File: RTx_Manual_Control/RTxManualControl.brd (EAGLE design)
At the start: 160 x 100 mm, 15 parts

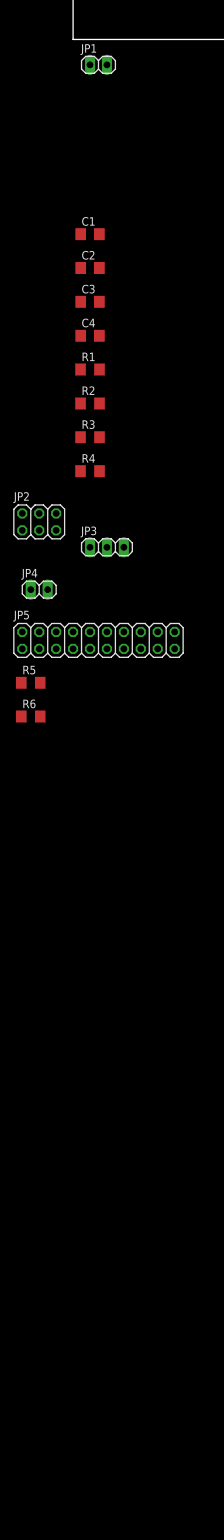
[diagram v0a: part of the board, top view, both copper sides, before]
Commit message: Completed draft of schematic without LPF component values. Need to determine LPF values, verify processor pinouts.
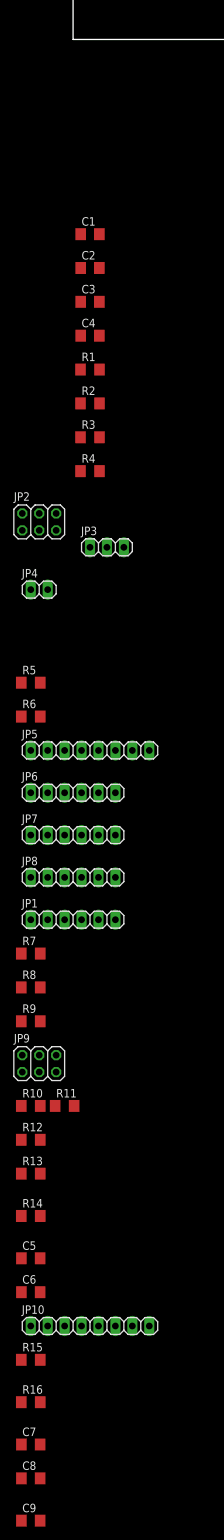
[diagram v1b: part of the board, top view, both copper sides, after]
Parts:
- added C5, C6: (no value), rcl:C1206
- added C7, C8, C9: 1uF, rcl:C1206
- added JP10: CON3, pinhead:1X08
- added JP6: CON2, pinhead:1X06
- added JP7: Main Axis Inputs, pinhead:1X06
- added JP8: Aux Axis Inputs, pinhead:1X06
- added JP9: Aux Switch/LEDs, pinhead:2X03
- added R10, R11, R7, R8: (no value), rcl:R1206
- added R12, R13, R9: 1k, rcl:R1206
- added R14, R15, R16: 10k, rcl:R1206
- JP1: value (none) -> CON1; device pinhead:1X02 -> pinhead:1X06
- JP2: value (none) -> Mode Switch/LEDs
- JP3: value (none) -> Neutral LEDs
- JP4: value (none) -> Drive Enable
- JP5: value (none) -> CON4; device pinhead:2X10 -> pinhead:1X08
- moved JP1 128.3 mm to (0.00, -132.1)
- moved JP5 16.6 mm to (2.54, -106.7)
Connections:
- removed net CH1_ADC: C1.1, R1.2
- removed net CH2_ADC: C2.1, R2.2
- removed net CH3_ADC: C3.1, R3.2
- removed net CH4_ADC: C4.1, R4.2
- removed net N$1: JP3.3, R6.2
- removed net N$2: JP3.2, R5.2
- new net +3.3V: C5.1, JP1.2, R12.2, R13.2, R9.2
- new net AREF: JP5.1, JP7.3, JP7.4, JP8.3, JP8.4
- new net AUX1_LED: JP6.1, R10.2
- new net AUX1_LED_CONN: JP9.2, R10.1
- new net AUX2_LED: JP6.4, R11.2
- new net AUX2_LED_CONN: JP9.6, R11.1
- new net AUX_SWITCH_IN: C7.1, JP10.6, JP9.1, R15.2
- new net AUX_SWITCH_PULLUP: JP9.3, R12.1
- new net AXIS3_ADC: C3.1, JP6.2, R3.2
- new net AXIS3_CONN: JP8.5, R3.1
- new net AXIS4_ADC: C4.1, JP6.3, R4.2
- new net AXIS4_CONN: JP8.2, R4.1
- new net DRIVE_ENABLE_IN: C9.1, JP4.2, JP5.4, R14.2
- new net DRIVE_ENABLE_PULLUP: JP4.1, R13.1
- new net LAT_AXIS_ADC: C2.1, JP5.6, R2.2
- new net LAT_AXIS_CONN: JP7.2, R2.1
- new net LAT_NEAUTRAL_LED_CONN: JP3.3, R6.1
- new net LAT_NEUTRAL_LED: JP6.6, R6.2
- new net MODE1_LED: JP5.7, R7.2
- new net MODE1_LED_CONN: JP2.2, R7.1
- new net MODE2_LED: JP5.8, R8.2
- new net MODE2_LED_CONN: JP2.6, R8.1
- new net MODE_SWITCH_IN: C8.1, JP10.4, JP2.5, R16.2
- new net MODE_SWITCH_PULLUP: JP2.3, R9.1
- new net VERT_AXIS_ADC: C1.1, JP5.3, R1.2
- new net VERT_AXIS_CONN: JP7.5, R1.1
- new net VERT_NEUTRAL_LED: JP6.5, R5.2
- new net VERT_NEUTRAL_LED_CONN: JP3.2, R5.1
- net +5V: now also C6.1, JP1.3, JP2.4, JP9.4
- net GND: now also C5.2, C6.2, C7.2, C8.2, C9.2, JP1.4, JP1.5, JP5.2, JP7.1, JP7.6, JP8.1, JP8.6, R14.1, R15.1, R16.1

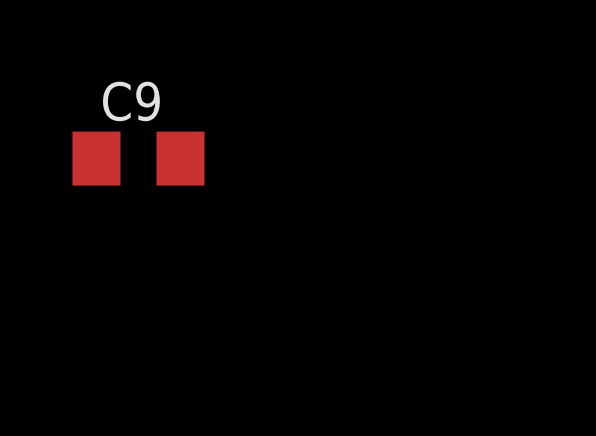
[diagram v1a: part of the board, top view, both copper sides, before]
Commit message: Changed pinout of Neutral LED connector. Added supply rail decoupling cap values, ARef decoupling cap.
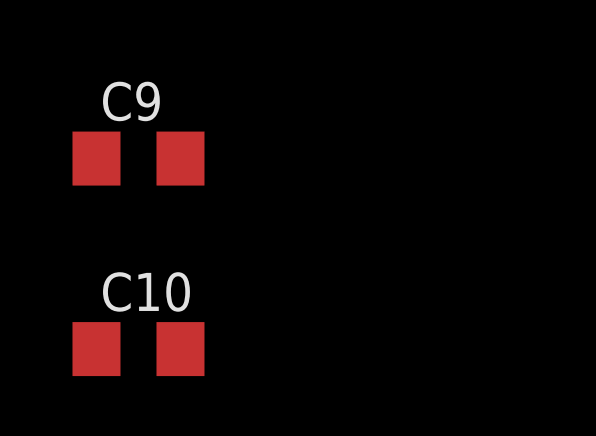
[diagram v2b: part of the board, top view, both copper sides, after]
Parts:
- added C10: 10uF, rcl:C1206
- C5, C6: value (none) -> 10uF
- R10, R11, R5, R6, R7, R8: value (none) -> 280
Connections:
- net +5V: now also JP3.2; no longer JP3.1
- net AREF: now also C10.1
- net GND: now also C10.2
- net VERT_NEUTRAL_LED_CONN: now also JP3.1; no longer JP3.2
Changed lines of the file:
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@@
 <element name="JP2" library="pinhead" package="2X03" value="Mode Switch/LEDs" x="-5.08" y="-72.39"/>
 <element name="JP4" library="pinhead" package="1X02" value="Drive Enable" x="-5.08" y="-82.55"/>
-<element name="R5" library="rcl" package="R1206" value="" x="-6.35" y="-96.52"/>
-<element name="R6" library="rcl" package="R1206" value="" x="-6.35" y="-101.6"/>
+<element name="R5" library="rcl" package="R1206" value="280" x="-6.35" y="-96.52"/>
+<element name="R6" library="rcl" package="R1206" value="280" x="-6.35" y="-101.6"/>
 <element name="JP5" library="pinhead" package="1X08" value="CON4" x="2.54" y="-106.68"/>
 <element name="JP6" library="pinhead" package="1X06" value="CON2" x="0" y="-113.03"/>
@@
 <element name="JP8" library="pinhead" package="1X06" value="Aux Axis Inputs" x="0" y="-125.73"/>
 <element name="JP1" library="pinhead" package="1X06" value="CON1" x="0" y="-132.08"/>
-<element name="R7" library="rcl" package="R1206" value="" x="-6.35" y="-137.16"/>
-<element name="R8" library="rcl" package="R1206" value="" x="-6.35" y="-142.24"/>
+<element name="R7" library="rcl" package="R1206" value="280" x="-6.35" y="-137.16"/>
+<element name="R8" library="rcl" package="R1206" value="280" x="-6.35" y="-142.24"/>
 <element name="R9" library="rcl" package="R1206" value="1k" x="-6.35" y="-147.32"/>
 <element name="JP9" library="pinhead" package="2X03" value="Aux Switch/LEDs" x="-5.08" y="-153.67"/>
-<element name="R10" library="rcl" package="R1206" value="" x="-6.35" y="-160.02"/>
-<element name="R11" library="rcl" package="R1206" value="" x="-1.27" y="-160.02"/>
+<element name="R10" library="rcl" package="R1206" value="280" x="-6.35" y="-160.02"/>
+<element name="R11" library="rcl" package="R1206" value="280" x="-1.27" y="-160.02"/>
 <element name="R12" library="rcl" package="R1206" value="1k" x="-6.35" y="-165.1"/>
 <element name="R13" library="rcl" package="R1206" value="1k" x="-6.35" y="-170.18"/>
 <element name="R14" library="rcl" package="R1206" value="10k" x="-6.35" y="-176.53"/>
-<element name="C5" library="rcl" package="C1206" value="" x="-6.35" y="-182.88"/>
-<element name="C6" library="rcl" package="C1206" value="" x="-6.35" y="-187.96"/>
+<element name="C5" library="rcl" package="C1206" value="10uF" x="-6.35" y="-182.88"/>
+<element name="C6" library="rcl" package="C1206" value="10uF" x="-6.35" y="-187.96"/>
 <element name="JP10" library="pinhead" package="1X08" value="CON3" x="2.54" y="-193.04"/>
 <element name="R15" library="rcl" package="R1206" value="10k" x="-6.35" y="-198.12"/>
@@
 <element name="C8" library="rcl" package="C1206" value="1uF" x="-6.35" y="-215.9"/>
 <element name="C9" library="rcl" package="C1206" value="1uF" x="-6.35" y="-222.25"/>
+<element name="C10" library="rcl" package="C1206" value="10uF" x="-6.35" y="-228.6"/>
 </elements>
 <signals>
@@
 <contactref element="C7" pad="2"/>
 <contactref element="C9" pad="2"/>
+<contactref element="C10" pad="2"/>
+<wire x1="-4.95" y1="-222.25" x2="-4.95" y2="-228.6" width="0" layer="19" extent="1-1"/>
 <wire x1="-4.95" y1="-215.9" x2="-4.95" y2="-222.25" width="0" layer="19" extent="1-1"/>
 <wire x1="-4.95" y1="-210.82" x2="-4.95" y2="-215.9" width="0" layer="19" extent="1-1"/>
@@
 </signal>
 <signal name="VERT_NEUTRAL_LED_CONN">
-<contactref element="JP3" pad="2"/>
 <contactref element="R5" pad="1"/>
-<wire x1="5.08" y1="-76.2" x2="-7.772" y2="-96.52" width="0" layer="19" extent="1-1"/>
+<contactref element="JP3" pad="1"/>
+<wire x1="2.54" y1="-76.2" x2="-7.772" y2="-96.52" width="0" layer="19" extent="1-1"/>
 </signal>
 <signal name="+5V">
-<contactref element="JP3" pad="1"/>
 <contactref element="JP1" pad="3"/>
 <contactref element="JP2" pad="4"/>
 <contactref element="JP9" pad="4"/>
 <contactref element="C6" pad="1"/>
+<contactref element="JP3" pad="2"/>
 <wire x1="-5.08" y1="-152.4" x2="-7.75" y2="-187.96" width="0" layer="19" extent="1-1"/>
 <wire x1="-1.27" y1="-132.08" x2="-5.08" y2="-152.4" width="0" layer="19" extent="1-1"/>
-<wire x1="2.54" y1="-76.2" x2="-1.27" y2="-132.08" width="0" layer="19" extent="1-1"/>
-<wire x1="-5.08" y1="-71.12" x2="2.54" y2="-76.2" width="0" layer="19" extent="1-1"/>
+<wire x1="5.08" y1="-76.2" x2="-1.27" y2="-132.08" width="0" layer="19" extent="1-1"/>
+<wire x1="-5.08" y1="-71.12" x2="5.08" y2="-76.2" width="0" layer="19" extent="1-1"/>
 </signal>
 <signal name="VERT_AXIS_CONN">
@@
 <contactref element="JP8" pad="3"/>
 <contactref element="JP8" pad="4"/>
+<contactref element="C10" pad="1"/>
+<wire x1="-1.27" y1="-125.73" x2="-7.75" y2="-228.6" width="0" layer="19" extent="1-1"/>
 <wire x1="1.27" y1="-125.73" x2="-1.27" y2="-125.73" width="0" layer="19" extent="1-1"/>
 <wire x1="-1.27" y1="-119.38" x2="-1.27" y2="-125.73" width="0" layer="19" extent="1-1"/>

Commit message: updated WPR.Updated RTx manual remote PCB.
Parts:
- moved C10 287.2 mm to (75.3, 46.7), turned to 90 degrees
- moved C8 286.5 mm to (79.5, 57.4), turned to 270 degrees
- moved C9 278.9 mm to (68.3, 46.5), turned to 270 degrees
- moved C7 278.5 mm to (67.8, 57.7), turned to 270 degrees
- moved R16 274.4 mm to (75.6, 57.4), turned to 90 degrees
- moved JP10 267.2 mm to (74.3, 64.4), flipped to the bottom
- moved R15 267.1 mm to (70.5, 57.7), turned to 90 degrees
- moved C6 247.6 mm to (92.1, 39.2), turned to 180 degrees
- moved R14 234.2 mm to (65.5, 46.4), turned to 90 degrees
- moved C5 221.9 mm to (58.4, 29.3), turned to 90 degrees
- moved R8 211.1 mm to (60.3, 58.0), turned to 90 degrees
- moved R13 208.8 mm to (55.2, 29.3), turned to 270 degrees
- moved R12 207.1 mm to (65.0, 29.3), turned to 270 degrees
- moved R7 205.6 mm to (57.8, 58.2), turned to 90 degrees
- moved R11 203.8 mm to (78.1, 27.7), turned to 270 degrees
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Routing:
- net +5V: track 0.00 -> 74.2 mm, vias 0 -> 1
- net AREF: track 0.00 -> 62.3 mm
- net AUX_SWITCH_IN: track 0.00 -> 55.4 mm, vias 0 -> 2
- net MODE1_LED_CONN: track 0.00 -> 52.2 mm, vias 0 -> 1
- net MODE2_LED_CONN: track 0.00 -> 40.6 mm, vias 0 -> 2
- net MODE_SWITCH_PULLUP: track 0.00 -> 39.3 mm, vias 0 -> 1
- net DRIVE_ENABLE_IN: track 0.00 -> 37.4 mm
- net AUX2_LED_CONN: track 0.00 -> 33.8 mm, vias 0 -> 1
- net AUX_SWITCH_PULLUP: track 0.00 -> 31.0 mm, vias 0 -> 2
- net MODE_SWITCH_IN: track 0.00 -> 30.0 mm
- net DRIVE_ENABLE_PULLUP: track 0.00 -> 28.5 mm, vias 0 -> 1
- net AUX1_LED_CONN: track 0.00 -> 23.4 mm, vias 0 -> 1
- net +3.3V: track 0.00 -> 16.5 mm
- net AXIS4_ADC: track 0.00 -> 15.8 mm
- net VERT_AXIS_CONN: track 0.00 -> 15.8 mm
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- added copper zone on layer 1, net GND
- added copper zone on layer 16, net GND
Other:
- board size 160 x 100 mm -> 58.4 x 49.4 mm
- board text added: "Manual Remote"
- board text added: "RocketTracks"

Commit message: Completed board layout. Ready for design review.
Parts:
- moved R5 49.5 mm to (41.8, 9.27), turned to 270 degrees
- moved R6 44.8 mm to (44.3, 9.27), turned to 270 degrees
- moved C8 44.2 mm to (39.4, 39.0)
- moved C4 43.8 mm to (39.2, 16.0)
- moved R4 43.7 mm to (36.8, 16.0)
- moved C3 43.1 mm to (32.9, 14.9)
- moved C10 43.0 mm to (36.4, 28.3)
- moved JP2 43.0 mm to (50.8, 30.4)
- moved C1 43.0 mm to (6.22, 39.8)
- moved C2 43.0 mm to (13.7, 39.8)
- moved C5 43.0 mm to (19.6, 10.9)
- moved JP10 43.0 mm to (35.4, 46.0)
- moved JP3 43.0 mm to (52.1, 13.8)
- moved JP5 43.0 mm to (12.6, 46.0)
- moved JP7 43.0 mm to (10.4, 23.5)
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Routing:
- net VERT_NEUTRAL_LED: track 14.5 -> 5.05 mm
- net VERT_NEUTRAL_LED_CONN: track 5.31 -> 13.7 mm
- net AXIS3_CONN: track 14.1 -> 6.14 mm
- net MODE1_LED_CONN: track 52.2 -> 47.4 mm
- net LAT_NEUTRAL_LED: track 8.68 -> 5.05 mm
- net LAT_NEAUTRAL_LED_CONN: track 5.31 -> 8.00 mm
- net AXIS3_ADC: track 12.0 -> 14.5 mm
- net AUX_SWITCH_IN: track 55.4 -> 53.3 mm
- net MODE_SWITCH_IN: track 30.0 -> 28.4 mm
- net AXIS4_ADC: track 15.8 -> 14.3 mm
- net AXIS4_CONN: track 5.39 -> 6.84 mm
- net +5V: track 74.2 -> 73.0 mm
- net AUX1_LED: track 4.04 -> 5.05 mm
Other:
- board size 58.4 x 49.4 mm -> 58.4 x 49 mm
